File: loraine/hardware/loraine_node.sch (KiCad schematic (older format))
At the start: 41 parts, among them CON1 BARREL_JACK, IC1 ATTINY2313A-S, P1 POWER_THRU, P2 POWER, P3 SOLDER_PAD, P4 ICSP, P5 OUTPUTS, P6 BUS, P7 BUS_THRU, Q1 BD679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

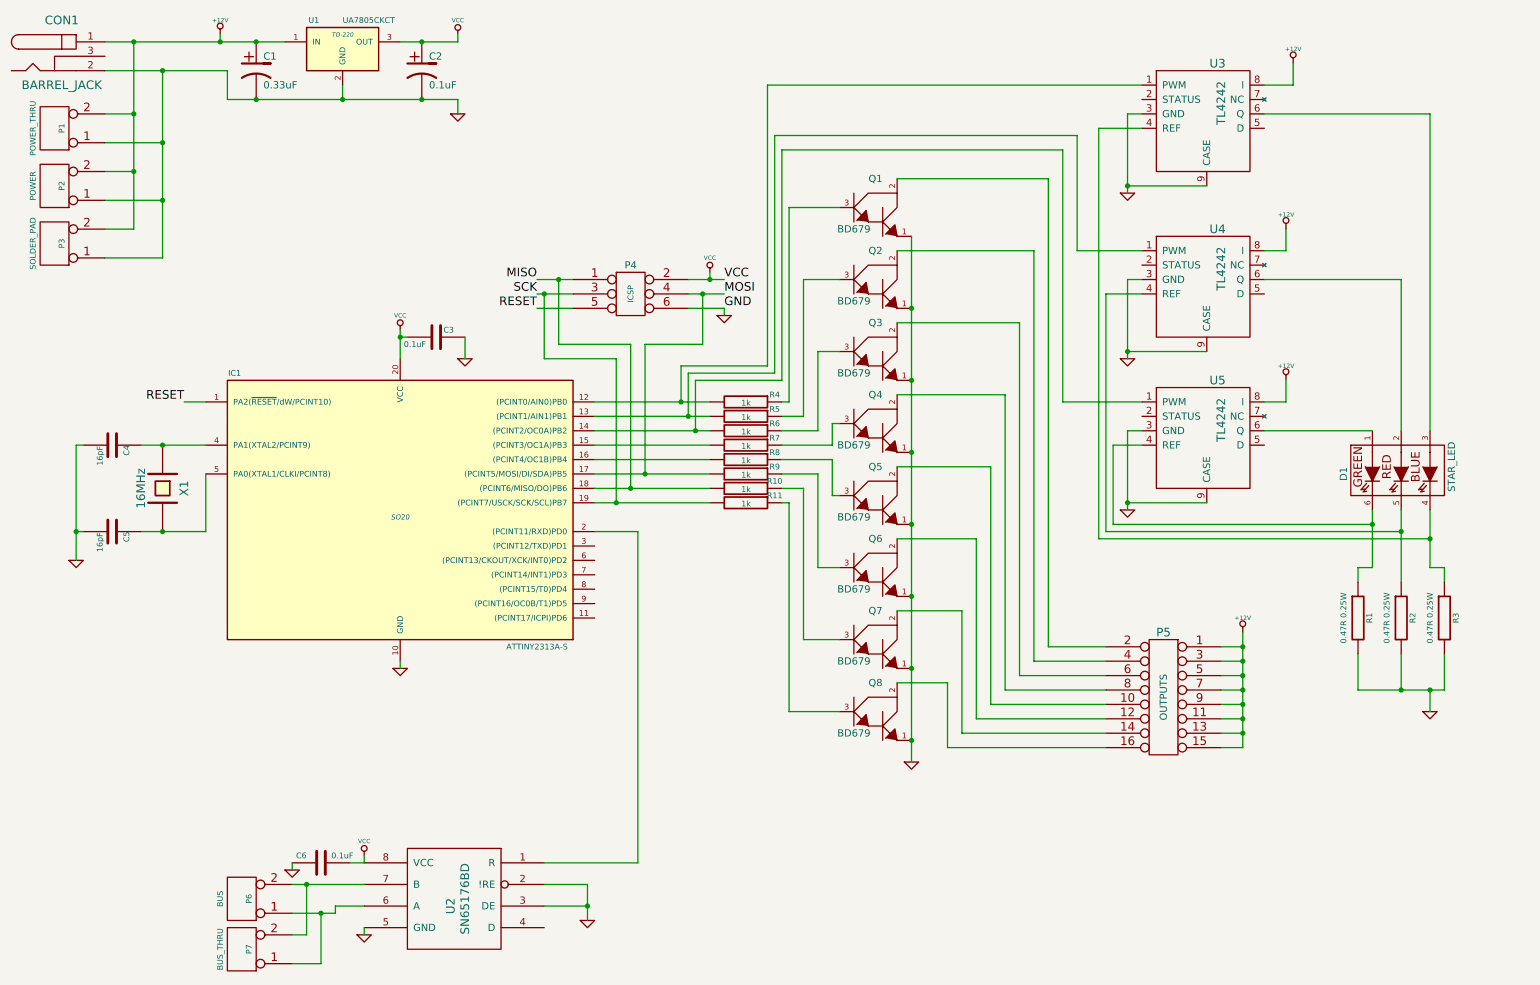
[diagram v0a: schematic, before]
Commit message: Fixed sense resistors in schematic
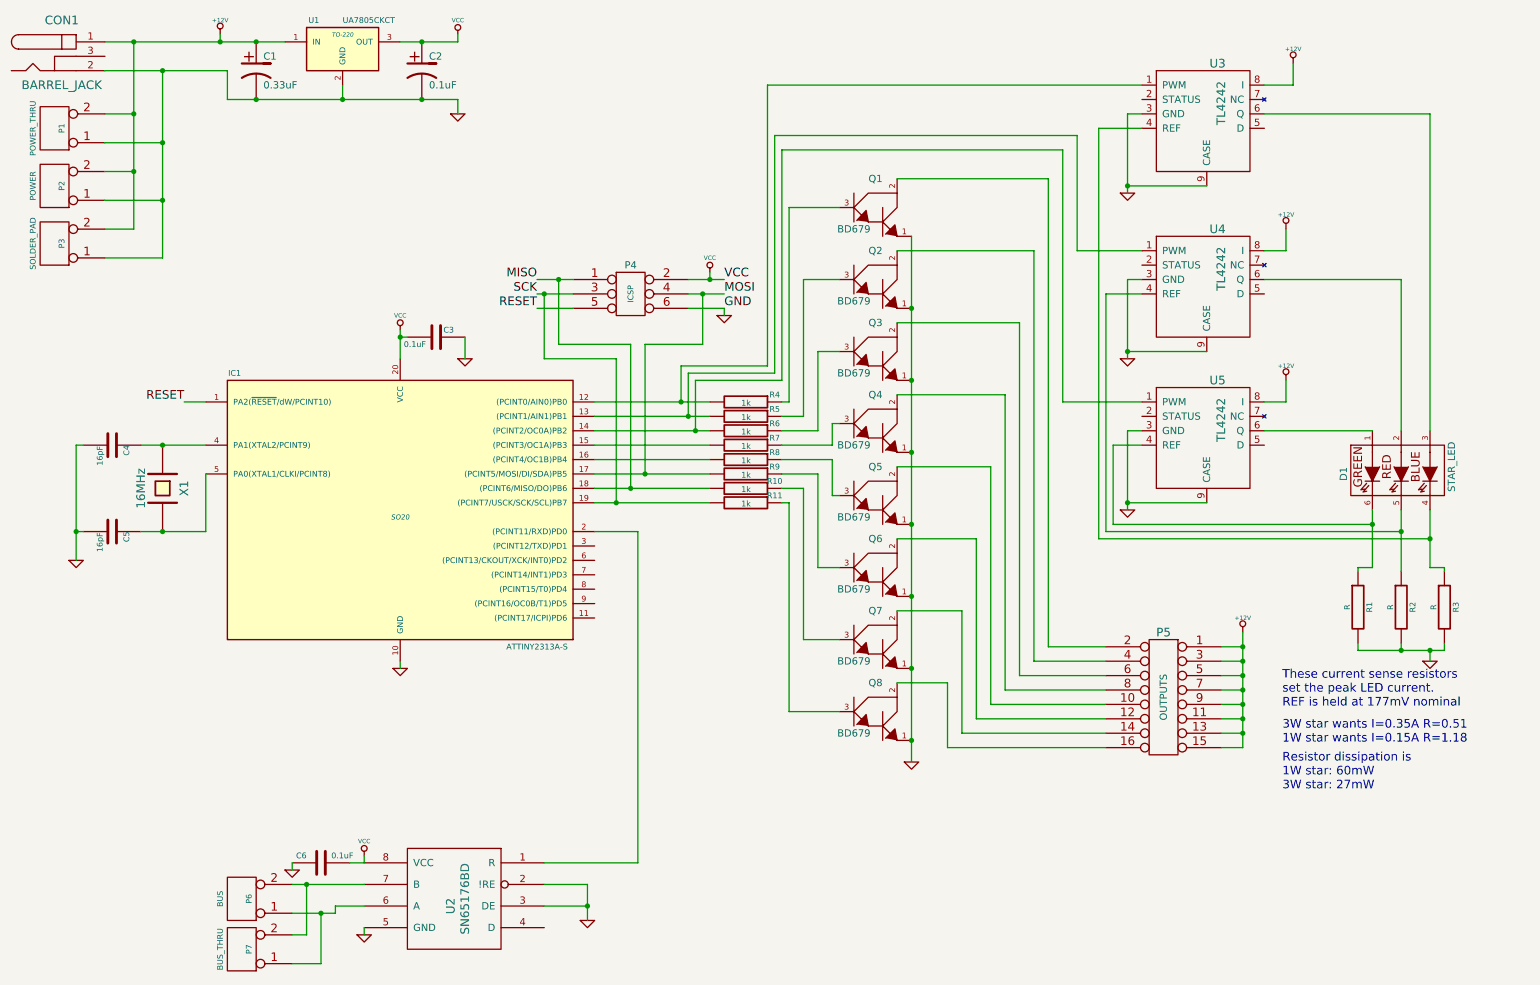
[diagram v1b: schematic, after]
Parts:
- R1, R2, R3: value 0.47R 0.25W -> R
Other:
- note added: "3W star wants I=0.35A R=0.51\n1W star wants I=0.15A R=1.18"
- note added: "Resistor dissipation is\n1W star: 60mW\n3W star: 27mW"
- note added: "These current sense resistors\nset the peak LED current.\nREF is held at 177mV nominal\n"
- moved on the sheet: R1, R2, R3
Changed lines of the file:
@@
 $EndComp
 Wire Wire Line
-	1650 3950 2100 3950
-Wire Wire Line
-	1650 4550 2100 4550
+	1650 3950 1800 3950
+Wire Wire Line
+	1800 3950 2100 3950
+Wire Wire Line
+	1650 4550 1800 4550
+Wire Wire Line
+	1800 4550 2100 4550
 Wire Wire Line
 	2100 4550 2100 4150
@@
 	1250 3950 1200 3950
 Wire Wire Line
-	1200 3950 1200 4750
+	1200 3950 1200 4550
+Wire Wire Line
+	1200 4550 1200 4750
 Wire Wire Line
 	1250 4550 1200 4550
@@
 Connection ~ 3600 1550
 Wire Wire Line
-	1400 1350 2250 1350
+	1400 1350 1800 1350
+Wire Wire Line
+	1800 1350 2250 1350
 Wire Wire Line
 	2250 1350 2250 1550
 Connection ~ 2200 1150
 Wire Wire Line
-	4800 3650 5600 3650
-Wire Wire Line
-	4800 3750 5600 3750
-Wire Wire Line
-	4800 3850 5600 3850
+	4800 3650 5400 3650
+Wire Wire Line
+	5400 3650 5600 3650
+Wire Wire Line
+	4800 3750 5450 3750
+Wire Wire Line
+	5450 3750 5600 3750
+Wire Wire Line
+	4800 3850 5500 3850
+Wire Wire Line
+	5500 3850 5600 3850
 Wire Wire Line
 	4800 3950 5600 3950
@@
 	4800 4050 5600 4050
 Wire Wire Line
-	4800 4150 5600 4150
-Wire Wire Line
-	4800 4250 5600 4250
-Wire Wire Line
-	4800 4350 5600 4350
+	4800 4150 5150 4150
+Wire Wire Line
+	5150 4150 5600 4150
+Wire Wire Line
+	4800 4250 5050 4250
+Wire Wire Line
+	5050 4250 5600 4250
+Wire Wire Line
+	4800 4350 4950 4350
+Wire Wire Line
+	4950 4350 5600 4350
 Wire Wire Line
 	6150 3650 6100 3650
@@
 	4450 7150 4750 7150
 Wire Wire Line
-	4750 7000 4750 7250
+	4750 7000 4750 7150
+Wire Wire Line
+	4750 7150 4750 7250
 Connection ~ 4750 7150
 Wire Wire Line
@@
 	7950 2100 7950 5350
 Wire Wire Line
-	2700 7000 3200 7000
+	2700 7000 2800 7000
+Wire Wire Line
+	2800 7000 3200 7000
 Connection ~ 3450 3200
 Wire Wire Line
 	3900 3200 3900 3350
 Wire Wire Line
-	1600 1150 1600 2450
+	1600 1150 1600 1650
+Wire Wire Line
+	1600 1650 1600 2050
+Wire Wire Line
+	1600 2050 1600 2450
 Connection ~ 1600 1150
 Wire Wire Line
@@
 	1400 1850 1800 1850
 Wire Wire Line
-	1800 1350 1800 2650
+	1800 1350 1800 1850
+Wire Wire Line
+	1800 1850 1800 2250
+Wire Wire Line
+	1800 2250 1800 2650
 Connection ~ 1800 1350
 Wire Wire Line
@@
 Connection ~ 5150 4150
 Wire Wire Line
-	4400 2800 4650 2800
-Wire Wire Line
-	4400 2900 4650 2900
+	4400 2800 4550 2800
+Wire Wire Line
+	4550 2800 4650 2800
+Wire Wire Line
+	4400 2900 4450 2900
+Wire Wire Line
+	4450 2900 4650 2900
 Wire Wire Line
 	4400 3000 4650 3000
 Wire Wire Line
-	5450 2800 5700 2800
-Wire Wire Line
-	5450 2900 5700 2900
+	5450 2800 5600 2800
+Wire Wire Line
+	5600 2800 5700 2800
+Wire Wire Line
+	5450 2900 5550 2900
+Wire Wire Line
+	5550 2900 5700 2900
 Wire Wire Line
 	5450 3000 5700 3000
@@
 	7450 4600 7450 5850
 Wire Wire Line
-	9300 5250 9300 6050
+	9300 5250 9300 5350
+Wire Wire Line
+	9300 5350 9300 5450
+Wire Wire Line
+	9300 5450 9300 5550
+Wire Wire Line
+	9300 5550 9300 5650
+Wire Wire Line
+	9300 5650 9300 5750
+Wire Wire Line
+	9300 5750 9300 5850
+Wire Wire Line
+	9300 5850 9300 5950
+Wire Wire Line
+	9300 5950 9300 6050
 Wire Wire Line
 	9300 5350 9150 5350
@@
 Connection ~ 9300 5950
 Wire Wire Line
-	1400 1150 2650 1150
+	1400 1150 1600 1150
+Wire Wire Line
+	1600 1150 2200 1150
+Wire Wire Line
+	2200 1150 2450 1150
+Wire Wire Line
+	2450 1150 2650 1150
 Connection ~ 2450 1150
 Connection ~ 2450 1550
 Wire Wire Line
-	2250 1550 3850 1550
-Wire Wire Line
-	3450 1150 3850 1150
+	2250 1550 2450 1550
+Wire Wire Line
+	2450 1550 3050 1550
+Wire Wire Line
+	3050 1550 3600 1550
+Wire Wire Line
+	3600 1550 3850 1550
+Wire Wire Line
+	3450 1150 3600 1150
+Wire Wire Line
+	3600 1150 3850 1150
 Wire Wire Line
 	3450 5450 3450 5500
@@
 	2200 1100 2200 1150
 Wire Wire Line
-	3450 3150 3450 3350
+	3450 3150 3450 3200
+Wire Wire Line
+	3450 3200 3450 3350
 Wire Wire Line
 	5600 2800 5600 2750
@@
 	3200 6850 3200 6800
 Wire Wire Line
-	7000 2500 7000 6150
+	7000 2500 7000 3000
+Wire Wire Line
+	7000 3000 7000 3500
+Wire Wire Line
+	7000 3500 7000 4000
+Wire Wire Line
+	7000 4000 7000 4500
+Wire Wire Line
+	7000 4500 7000 5000
+Wire Wire Line
+	7000 5000 7000 5500
+Wire Wire Line
+	7000 5500 7000 6000
+Wire Wire Line
+	7000 6000 7000 6150
 Wire Wire Line
 	6150 2300 6500 2300
@@
 	2700 6850 2700 6900
 Wire Wire Line
-	2700 7200 3000 7200
+	2700 7200 2900 7200
+Wire Wire Line
+	2900 7200 3000 7200
 Wire Wire Line
 	3000 7200 3000 7150
@@
 L GND #PWR016
 U 1 1 5339EE64
-P 10600 5800
-F 0 "#PWR016" H 10600 5800 30  0001 C CNN
-F 1 "GND" H 10600 5730 30  0001 C CNN
-F 2 "" H 10600 5800 60  0000 C CNN
-F 3 "" H 10600 5800 60  0000 C CNN
-	1    10600 5800
-	1    0    0    -1
-$EndComp
-Connection ~ 10400 5650
-Wire Wire Line
-	10600 5650 10600 5800
-Connection ~ 10600 5650
+P 10600 5450
+F 0 "#PWR016" H 10600 5450 30  0001 C CNN
+F 1 "GND" H 10600 5380 30  0001 C CNN
+F 2 "" H 10600 5450 60  0000 C CNN
+F 3 "" H 10600 5450 60  0000 C CNN
+	1    10600 5450
+	1    0    0    -1
+$EndComp
+Connection ~ 10400 5375
+Connection ~ 10600 5375
 Wire Wire Line
 	9450 3850 10200 3850
@@
 	9050 2150 8500 2150
 Wire Wire Line
-	8500 1650 8500 2200
+	8500 1650 8500 2150
+Wire Wire Line
+	8500 2150 8500 2200
 Wire Wire Line
 	8500 1650 8600 1650
@@
 $EndComp
 Wire Wire Line
-	8500 2800 8500 3350
+	8500 2800 8500 3300
+Wire Wire Line
+	8500 3300 8500 3350
 Wire Wire Line
 	8500 3300 9050 3300
@@
 $EndComp
 Wire Wire Line
-	8500 3850 8500 4400
+	8500 3850 8500 4350
+Wire Wire Line
+	8500 4350 8500 4400
 Wire Wire Line
 	8500 4350 9050 4350
@@
 L R R1
 U 1 1 5339FA1A
-P 10100 5150
-F 0 "R1" V 10180 5150 40  0000 C CNN
-F 1 "0.47R 0.25W" V 10000 5150 40  0000 C CNN
-F 2 "" V 10030 5150 30  0000 C CNN
-F 3 "" H 10100 5150 30  0000 C CNN
-	1    10100 5150
+P 10100 5075
+F 0 "R1" V 10180 5075 40  0000 C CNN
+F 1 "R" V 10025 5075 40  0000 C CNN
+F 2 "" V 10030 5075 30  0000 C CNN
+F 3 "" H 10100 5075 30  0000 C CNN
+	1    10100 5075
 	1    0    0    -1
 $EndComp
@@
 L R R2
 U 1 1 5339FA2E
-P 10400 5150
-F 0 "R2" V 10480 5150 40  0000 C CNN
-F 1 "0.47R 0.25W" V 10300 5150 40  0000 C CNN
-F 2 "" V 10330 5150 30  0000 C CNN
-F 3 "" H 10400 5150 30  0000 C CNN
-	1    10400 5150
+P 10400 5075
+F 0 "R2" V 10480 5075 40  0000 C CNN
+F 1 "R" V 10325 5075 40  0000 C CNN
+F 2 "" V 10330 5075 30  0000 C CNN
+F 3 "" H 10400 5075 30  0000 C CNN
+	1    10400 5075
 	1    0    0    -1
 $EndComp
@@
 L R R3
 U 1 1 5339FA42
-P 10700 5150
-F 0 "R3" V 10780 5150 40  0000 C CNN
-F 1 "0.47R 0.25W" V 10600 5150 40  0000 C CNN
-F 2 "" V 10630 5150 30  0000 C CNN
-F 3 "" H 10700 5150 30  0000 C CNN
-	1    10700 5150
+P 10700 5075
+F 0 "R3" V 10780 5075 40  0000 C CNN
+F 1 "R" V 10625 5075 40  0000 C CNN
+F 2 "" V 10630 5075 30  0000 C CNN
+F 3 "" H 10700 5075 30  0000 C CNN
+	1    10700 5075
 	1    0    0    -1
 $EndComp
@@
 Connection ~ 10400 4550
 Wire Wire Line
-	10400 4400 10400 4900
-Wire Wire Line
-	10400 5400 10400 5650
+	10400 4400 10400 4550
+Wire Wire Line
+	10400 4550 10400 4825
 $Comp
 L STAR_LED D1
@@
 $EndComp
 Wire Wire Line
-	10200 4400 10200 4800
+	10200 4400 10200 4500
+Wire Wire Line
+	10200 4500 10200 4800
 Connection ~ 10200 4500
 Wire Wire Line
 	8300 4600 10600 4600
 Wire Wire Line
-	10600 4400 10600 4800
+	10600 4400 10600 4600
+Wire Wire Line
+	10600 4600 10600 4800
 Connection ~ 10600 4600
 Wire Wire Line
@@
 	9450 1650 10600 1650
 Wire Wire Line
-	10100 5400 10100 5650
-Wire Wire Line
-	10100 5650 10700 5650
-Wire Wire Line
-	10700 5650 10700 5400
-Wire Wire Line
-	10100 4900 10100 4800
+	10100 5375 10400 5375
+Wire Wire Line
+	10400 5375 10600 5375
+Wire Wire Line
+	10600 5375 10700 5375
+Wire Wire Line
+	10100 4825 10100 4800
 Wire Wire Line
 	10100 4800 10200 4800
 Wire Wire Line
-	10700 4900 10700 4800
+	10700 4825 10700 4800
 Wire Wire Line
 	10700 4800 10600 4800
 Wire Wire Line
 	3500 3200 3450 3200
+Text Notes 9575 5775 0    60   ~ 0
+These current sense resistors\nset the peak LED current.\nREF is held at 177mV nominal\n
+Text Notes 9575 6025 0    60   ~ 0
+3W star wants I=0.35A R=0.51\n1W star wants I=0.15A R=1.18
+Text Notes 9575 6350 0    60   ~ 0
+Resistor dissipation is\n1W star: 60mW\n3W star: 27mW
+Wire Wire Line
+	10100 5325 10100 5375
+Wire Wire Line
+	10400 5375 10400 5325
+Wire Wire Line
+	10700 5375 10700 5325
+Wire Wire Line
+	10600 5375 10600 5450
 $EndSCHEMATC
